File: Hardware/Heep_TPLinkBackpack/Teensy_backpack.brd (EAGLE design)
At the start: 45 x 57.5 mm, 8 parts

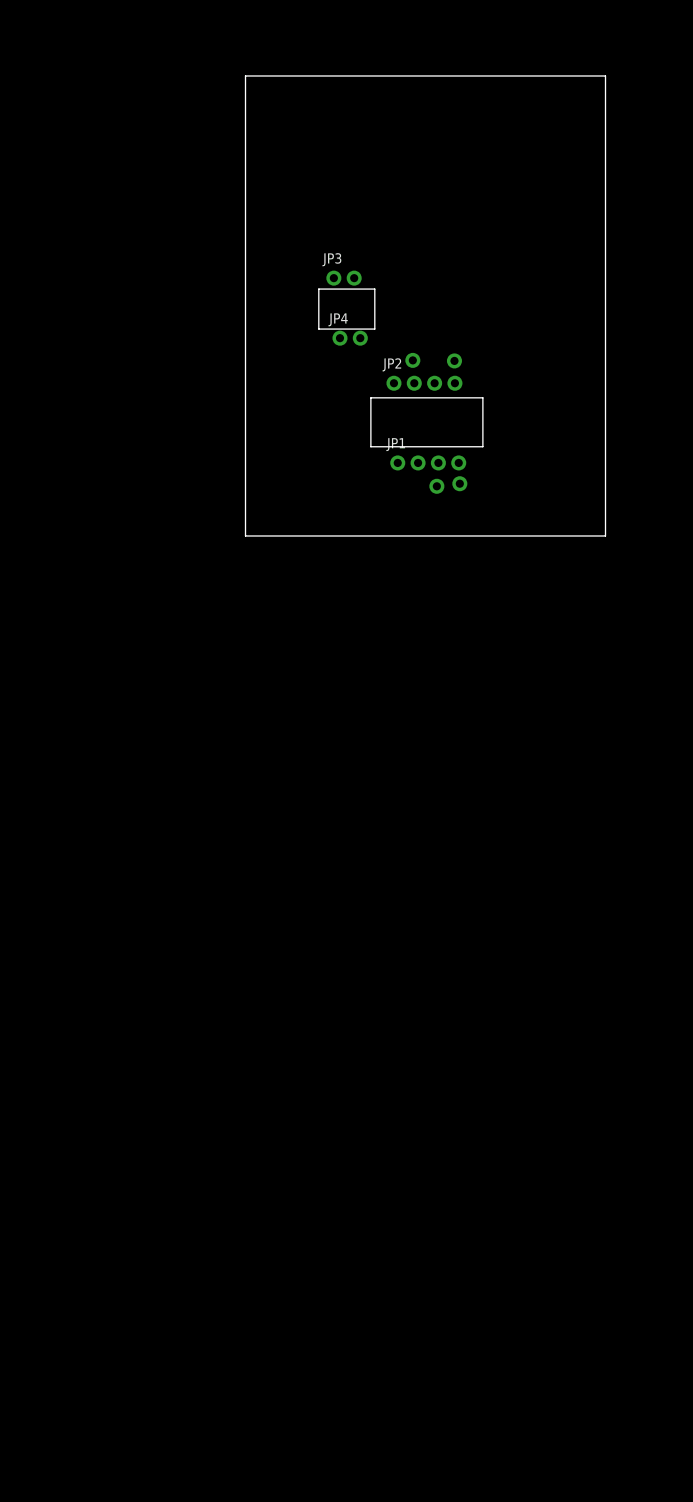
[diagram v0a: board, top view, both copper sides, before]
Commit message: #44 Added ENC, Teensy, and Turn on Circuitry
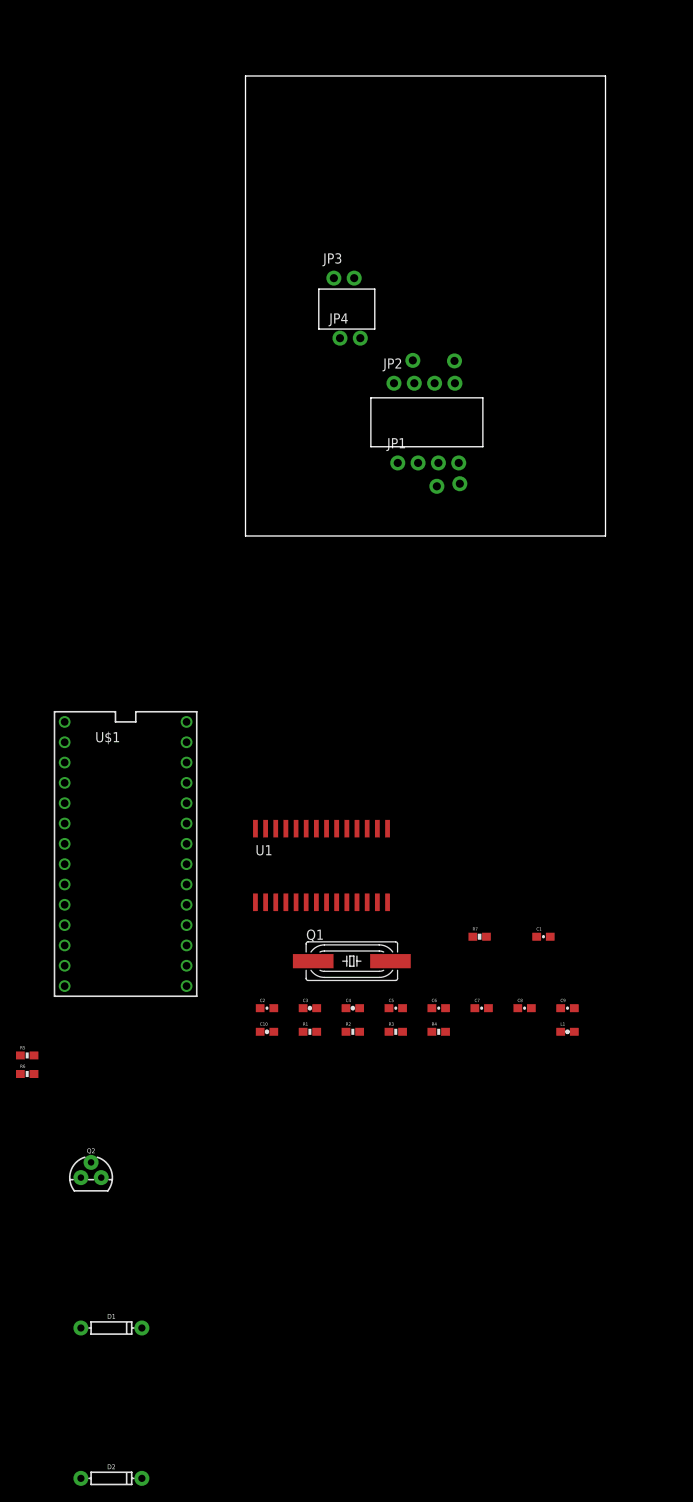
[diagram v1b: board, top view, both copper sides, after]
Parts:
- added C1, C2, C5, C6, C7, C8, C9: 0.1uF, SparkFun-Capacitors:0603-CAP
- added C10: 10uF, SparkFun-Passives:0603-CAP
- added C3, C4: 10pF, SparkFun-Passives:0603-CAP
- added D1, D2: 200mA/100V/1V, SparkFun-DiscreteSemi:DIODE-1N4148
- added L1: (no value), SparkFun-Passives:0603
- added Q1: 25MHz, adafruit:SM49
- added Q2: 600mA/40V, SparkFun-DiscreteSemi:TO-92
- added R1, R2, R3, R4: 51, SparkFun-Resistors:0603-RES
- added R5, R6: 10k, SparkFun-Resistors:0603-RES
- added R7: 2k @ 1% Tolerance, SparkFun-Passives:0603-RES
- added U$1: TEENSY_3.1-3.2_DIL, Teensy_3_and_LC_Series_Boards_v1.4:TEENSY_3.0-3.2&LC_DIL
- added U1: ENC28J60-SO, microchip-enc28j60:SO28W
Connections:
- removed net +3V3: JP3.2, JP4.2
- removed net RX+: JP1.4, JP7.1
- removed net RX-: JP2.4, JP5.1
- removed net TX+: JP1.3, JP8.1
- removed net TX-: JP2.2, JP6.1
- new net #CS: R5.1, U$1.10, U1.9
- new net #RESET: R6.1, U$1.2, U1.10
- new net 3.3V: C5.1, C6.1, C7.1, C8.1, C9.1, D2.A, JP3.2, JP4.2, L1.1, R5.2, R6.2, U$1.3.3V, U1.15, U1.19, U1.20, U1.25, U1.28
- new net AGND: JP3.1, JP4.1, Q2.3, U$1.AGND
- new net N$1: D1.A, D2.C
- new net N$12: C3.1, Q1.2, U1.23
- new net N$13: C4.1, Q1.1, U1.24
- new net N$15: R7.1, U1.14
- new net N$17: C10.2, U1.1
- new net N$2: D1.C, Q2.2
- new net N$5: C2.1, R3.1, R4.1
- new net N$7: C1.1, L1.2, R1.1, R2.1
- new net RD+: JP1.4, JP7.1, R3.2, U1.13
- new net RD-: JP2.4, JP5.1, R4.2, U1.12
- new net SCK: U$1.13, U1.8
- new net SI: U$1.11, U1.7
- new net SO: U$1.12, U1.6
- new net TD+: JP1.3, JP8.1, R2.2, U1.17
- new net TD-: JP2.2, JP6.1, R1.2, U1.16
- new net VIN: U$1.VIN
- net GND: now also C1.2, C10.1, C2.2, C3.2, C4.2, C5.2, C6.2, C7.2, C8.2, C9.2, Q2.1, R7.2, U$1.GND, U1.11, U1.18, U1.2, U1.21, U1.22; no longer JP3.1, JP4.1

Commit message: #44 Added parts to board
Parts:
- moved D2 151.3 mm to (6.46, 31.7), turned to 90 degrees
- moved D1 132.4 mm to (3.53, 31.8), turned to 270 degrees
- moved R6 123.6 mm to (15.9, 48.5), turned to 90 degrees
- moved R5 120.7 mm to (13.8, 48.5), turned to 90 degrees
- moved Q2 106.5 mm to (5.38, 23.4), turned to 90 degrees
- moved U$1 94.9 mm to (23.6, 46.9), turned to 90 degrees
- moved C3 93.7 mm to (29.3, 32.2)
- moved C4 91.3 mm to (19.1, 32.1), turned to 180 degrees
- moved L1 85.2 mm to (11.2, 18.2), turned to 180 degrees
- moved R7 83.3 mm to (42.0, 32.2), turned to 180 degrees
- moved R4 83.3 mm to (14.8, 20.8)
- moved Q1 82.1 mm to (24.3, 28.2)
- moved R1 81.2 mm to (14.8, 19.0)
- moved C10 79.5 mm to (43.3, 6.42), turned to 90 degrees
- moved C1 75.4 mm to (11.2, 20.6)
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
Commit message: #44 Reoganized the circuit board
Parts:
- removed C8, C9: 0.1uF, SparkFun-Capacitors:0603-CAP
- moved C5 29.4 mm to (43.4, 33.3), turned to 90 degrees
- moved C7 27.8 mm to (41.0, 33.3), turned to 90 degrees
- moved R7 27.1 mm to (33.3, 6.59), turned to 0 degrees
- moved C6 27.0 mm to (38.4, 33.3), turned to 90 degrees
- moved C10 24.2 mm to (28.7, 25.7), turned to 0 degrees
- moved C1 17.1 mm to (14.7, 3.87), turned to 180 degrees
- moved L1 12.5 mm to (14.6, 6.15), turned to 0 degrees
- moved C2 11.8 mm to (11.5, 3.84)
- moved R2 11.6 mm to (20.4, 6.12)
- moved R3 11.5 mm to (20.4, 4.15), turned to 0 degrees
- moved C4 11.4 mm to (30.4, 33.8), turned to 0 degrees
- moved C3 10.5 mm to (19.0, 33.8), turned to 180 degrees
- moved R4 7.11 mm to (8.47, 17.5)
- moved U1 3.88 mm to (36.9, 17.4), turned to 270 degrees
- moved R5 3.56 mm to (17.4, 48.0)
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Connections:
- net 3.3V: no longer C8.1, C9.1
- net GND: no longer C8.2, C9.2
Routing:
- added copper zone on layer 1, net GND

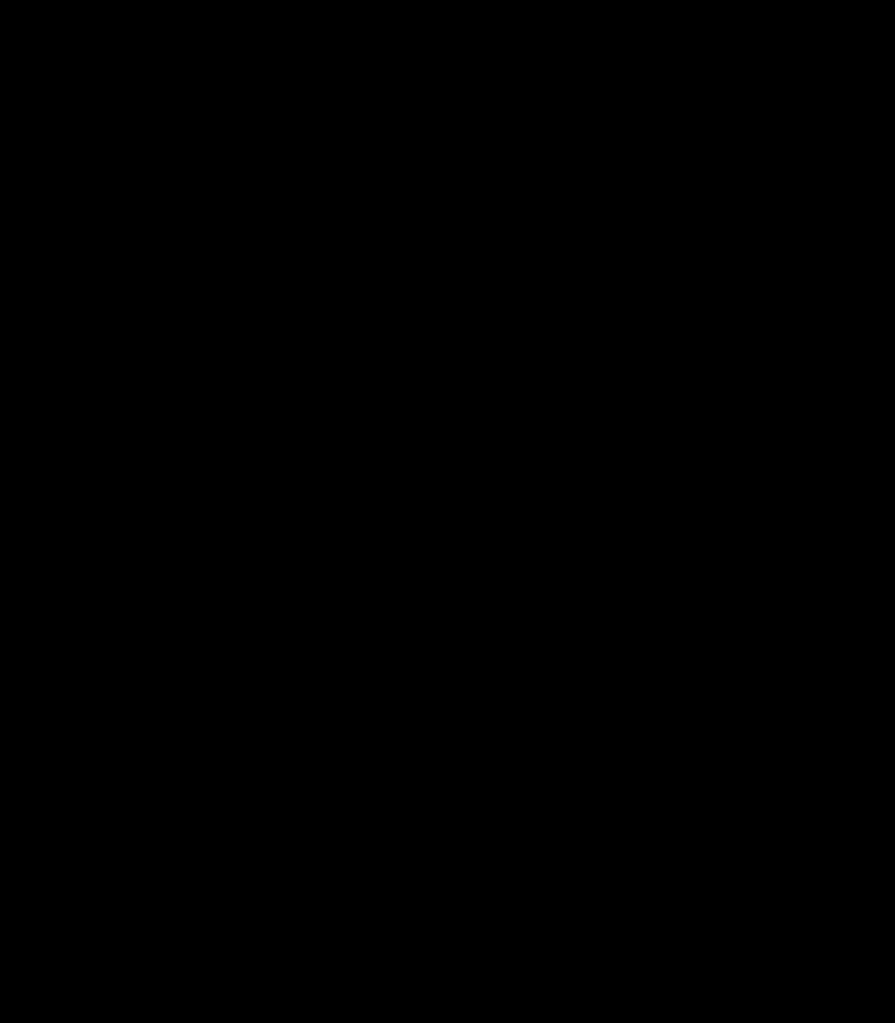
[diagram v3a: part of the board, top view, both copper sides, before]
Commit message: #44 Added turn on circuit
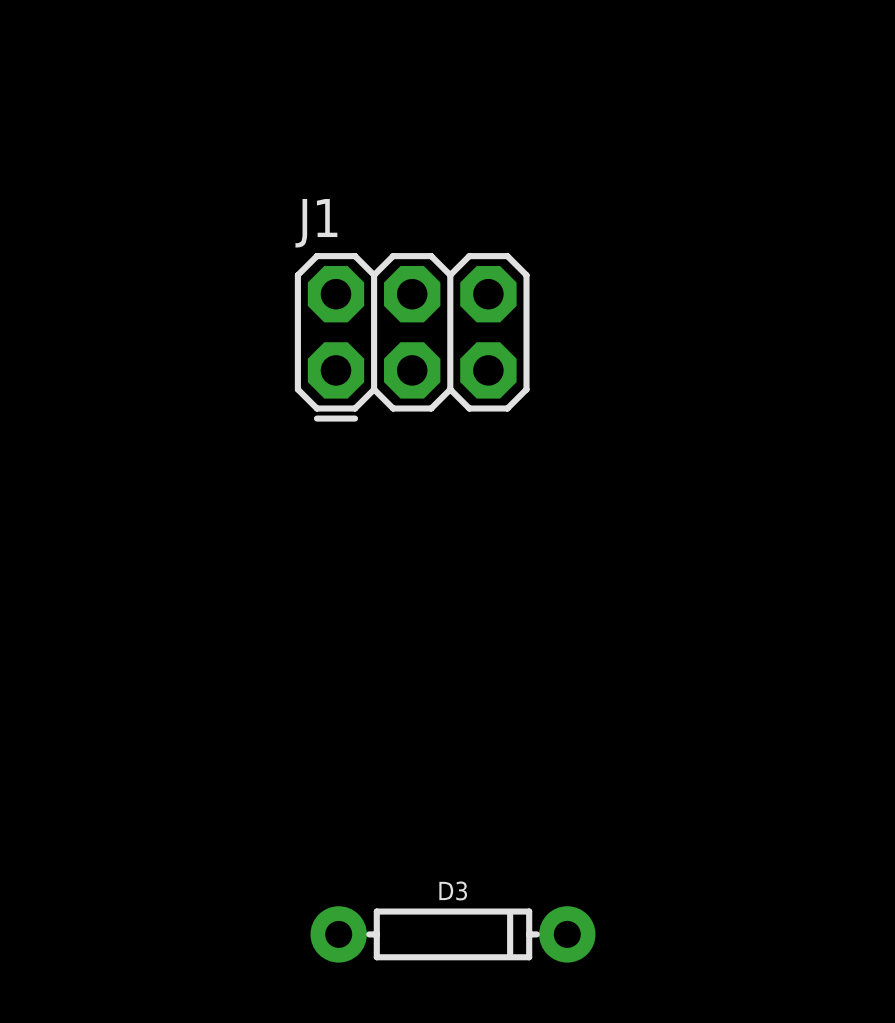
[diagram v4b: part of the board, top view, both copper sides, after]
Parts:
- added D3: 200mA/100V/1V, SparkFun-DiscreteSemi:DIODE-1N4148
- added J1: FEMALE 2x3, SparkFun-Connectors:2X3
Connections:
- new net N$3: D2.A, D3.C
- net 3.3V: now also D3.A; no longer D2.A
- net GND: now also J1.1, J1.2, J1.3, J1.4, J1.5, J1.6
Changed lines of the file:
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@@
 <attribute name="PROD_ID" value="DIO-08378" x="6.4551375" y="31.710490625" size="1.778" layer="27" rot="R90" display="off"/>
+</element>
+<element name="J1" library="SparkFun-Connectors" package="2X3" value="FEMALE 2x3" x="0.2" y="-35.2">
+<attribute name="PROD_ID" value="CONN-11566" x="0.2" y="-35.2" size="1.778" layer="27" display="off"/>
+</element>
+<element name="D3" library="SparkFun-DiscreteSemi" package="DIODE-1N4148" value="200mA/100V/1V" x="4.1" y="-54">
+<attribute name="PROD_ID" value="DIO-08378" x="4.1" y="-54" size="1.778" layer="27" display="off"/>
 </element>
 </elements>
@@
 <vertex x="-9" y="65"/>
 </polygon>
+<contactref element="J1" pad="1"/>
+<contactref element="J1" pad="3"/>
+<contactref element="J1" pad="5"/>
+<contactref element="J1" pad="2"/>
+<contactref element="J1" pad="4"/>
+<contactref element="J1" pad="6"/>
+<wire x1="2.74" y1="-35.2" x2="0.2" y2="-35.2" width="0" layer="19" extent="1-1"/>
+<wire x1="0.2" y1="-32.66" x2="0.2" y2="-35.2" width="0" layer="19" extent="1-1"/>
+<wire x1="5.28" y1="-35.2" x2="2.74" y2="-35.2" width="0" layer="19" extent="1-1"/>
+<wire x1="2.74" y1="-32.66" x2="2.74" y2="-35.2" width="0" layer="19" extent="1-1"/>
+<wire x1="5.28" y1="-32.66" x2="5.28" y2="-35.2" width="0" layer="19" extent="1-1"/>
+<wire x1="12.319009375" y1="3.84091875" x2="5.28" y2="-32.66" width="0" layer="19" extent="1-1"/>
 </signal>
 <signal name="RD+">
@@
 <contactref element="JP3" pad="2"/>
 <contactref element="JP4" pad="2"/>
-<contactref element="D2" pad="A"/>
+<contactref element="D3" pad="A"/>
 <wire x1="40.96240625" y1="32.410446875" x2="43.35735625" y2="32.441090625" width="0" layer="19" extent="1-1"/>
 <wire x1="38.408021875" y1="32.439575" x2="40.96240625" y2="32.410446875" width="0" layer="19" extent="1-1"/>
@@
 <wire x1="13.592059375" y1="32.23163125" x2="38.408021875" y2="32.439575" width="0" layer="19" extent="1-1"/>
 <wire x1="14.35696875" y1="24.729321875" x2="13.592059375" y2="32.23163125" width="0" layer="19" extent="1-1"/>
-<wire x1="6.4551375" y1="27.900490625" x2="13.592059375" y2="32.23163125" width="0" layer="19" extent="1-1"/>
 <wire x1="12.12285" y1="48.7206375" x2="13.592059375" y2="32.23163125" width="0" layer="19" extent="1-1"/>
 <wire x1="17.361953125" y1="48.824065625" x2="12.12285" y2="48.7206375" width="0" layer="19" extent="1-1"/>
 <wire x1="12.158478125" y1="54.563021875" x2="12.12285" y2="48.7206375" width="0" layer="19" extent="1-1"/>
 <wire x1="13.78765" y1="6.147840625" x2="14.35696875" y2="24.729321875" width="0" layer="19" extent="1-1"/>
+<wire x1="0.29" y1="-54" x2="13.78765" y2="6.147840625" width="0" layer="19" extent="1-1"/>
 </signal>
 <signal name="N$15">
@@
 <wire x1="3.478028125" y1="23.369240625" x2="3.5312" y2="28.009928125" width="0" layer="19" extent="1-1"/>
 </signal>
+<signal name="N$3">
+<contactref element="D3" pad="C"/>
+<contactref element="D2" pad="A"/>
+<wire x1="6.4551375" y1="27.900490625" x2="7.91" y2="-54" width="0" layer="19" extent="1-1"/>
+</signal>
 </signals>
